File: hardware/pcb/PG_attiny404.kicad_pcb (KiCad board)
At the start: 2 copper layers, 20.3 x 59.7 mm, 28 parts, among them J1 0022232041, J2 Conn_01x01_Male, J3 Conn_01x01_Male, J4 Conn_01x01_Male, J5 Conn_01x01_Male, J6 Conn_01x01_Male, J7 Conn_01x01_Male, J8 Conn_01x01_Male, Q1 2N7002, SW1 SW_Push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

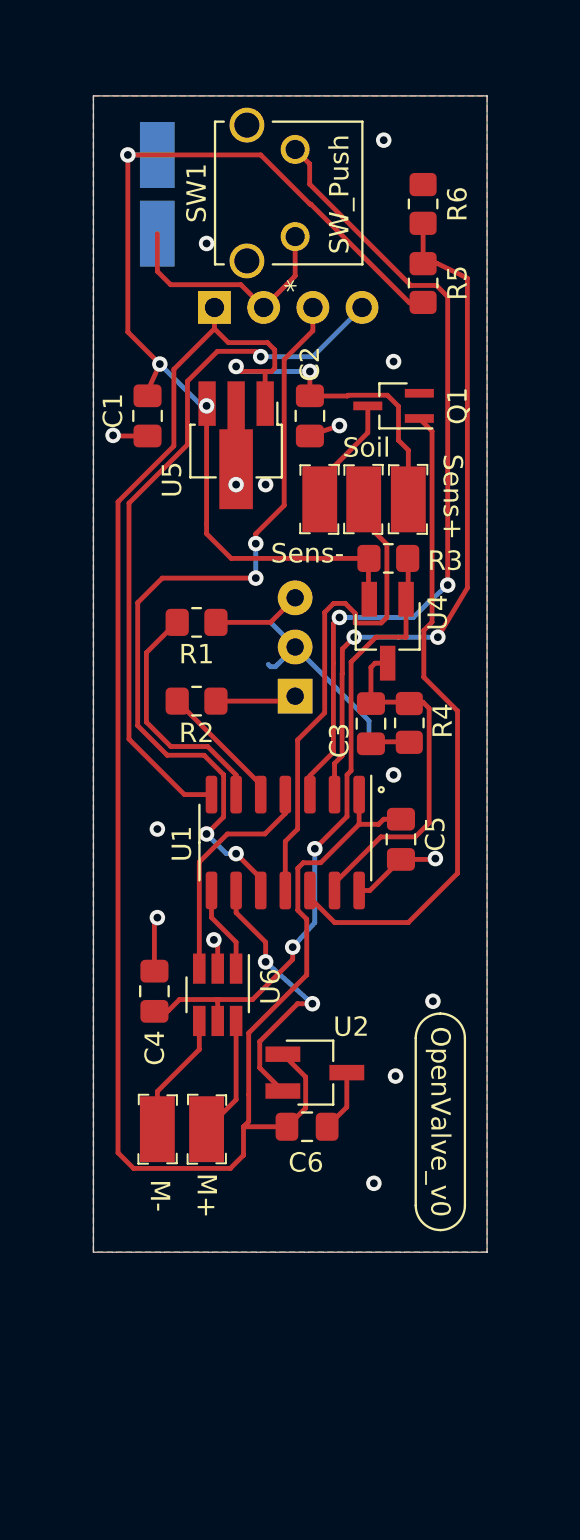
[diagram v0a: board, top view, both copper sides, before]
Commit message: Equiped PCB with additional led, changed other led, changed position of solder pads and side of hall sensor
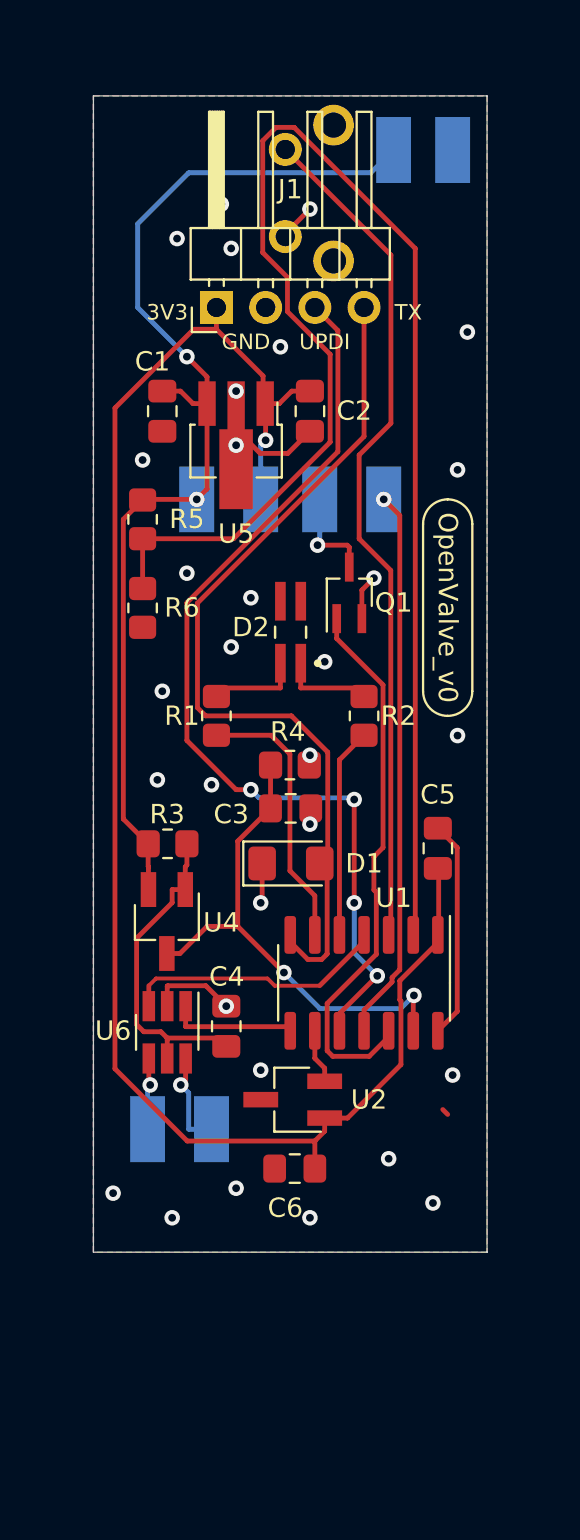
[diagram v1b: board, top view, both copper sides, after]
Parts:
- removed U3: XLUGR34M, LED_THT:LED_D3.0mm-3
- added D1: APTD3216QBC/D, LED_SMD:LED_1206_3216Metric_Pad1.42x1.75mm_HandSolder, F.Cu at (132.1, 106.9)
- added D2: XZMDKVG55W-8, XZMDKVG55W-8:LED_XZMDKVG55W-8, F.Cu at (132.1, 95.0)
- added J9: Conn_01x01_Male, digikey-footprints:PROBE_PAD_1206, B.Cu at (127.3, 88.1)
- J1: footprint Connector_PinSocket_2.54mm:PinSocket_1x04_P2.54mm_Horizontal -> Connector_PinHeader_2.54mm:PinHeader_1x04_P2.54mm_Horizontal; moved to F.Cu
- J4, J5, J6, J7, J8, SW1: moved to B.Cu
- R1, R2: value 100 Ohm -> 56 Ohm
- R5: value 200k -> 2M
- R6: value 100k -> 1M
- moved R6 25.4 mm to (124.5, 93.7), turned to -90 degrees
- moved R5 18.9 mm to (124.5, 89.2), turned to -90 degrees
- moved U4 18.8 mm to (125.7, 109.9)
- moved R3 18.6 mm to (125.7, 105.9)
- moved J2 15.8 mm to (140.5, 70.1)
- moved J3 12.2 mm to (137.4, 70.1)
- moved Q1 9.92 mm to (135.1, 93.0), turned to 90 degrees
- moved R2 8.68 mm to (135.9, 99.3), turned to -90 degrees
- moved U1 8.30 mm to (135.9, 113.1)
- moved J4 7.62 mm to (130.6, 88.1)
- moved R4 6.54 mm to (132.1, 101.9), turned to 180 degrees
- moved C3 6.02 mm to (132.1, 104.1), turned to 180 degrees
- moved R1 4.93 mm to (128.3, 99.3), turned to -90 degrees
- moved C4 4.13 mm to (128.8, 115.3)
- moved U6 3.25 mm to (125.7, 115.7)
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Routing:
- net /BatterySensing: track 36.3 -> 77.5 mm, vias 2 -> 0
- net +3V3: track 107.5 -> 85.2 mm, vias 2 -> 1
- net Net-(U4-Vs-): track 33.4 -> 17.0 mm, vias 2 -> 0
- net GND: track 44.5 -> 29.9 mm, vias 15 -> 31
- net /Hall: track 14.1 -> 2.82 mm, vias 2 -> 0
- net /UART_TX: track 36.0 -> 45.4 mm, vias 1 -> 0
- net /CurrentSensing: track 18.3 -> 26.2 mm, vias 0 -> 2
- net /UPDI: track 41.4 -> 49.2 mm
- net /SoilSensorOn: track 34.2 -> 28.6 mm
- net /LED_R: track 6.61 -> 10.8 mm
- net +BATT: track 54.1 -> 57.2 mm, vias 3 -> 2
- net Net-(J8-Pin_1): track 6.48 -> 3.74 mm, vias 0 -> 1
- net /Soilmoisture: track 26.0 -> 28.5 mm, vias 0 -> 1
- net /Motor+: track 4.56 -> 6.55 mm
- net /Motor-: track 12.0 -> 13.8 mm
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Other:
- board text added: "3.3V"
- board text added: "9V"
- board text removed: "G"
- board text removed: "R"
- board text removed: "Sens+"
- board text removed: "Sens-"

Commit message: Added Reverse voltage protection on PCB
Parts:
- added MOSFET1: SSM3J338R_LF, SOT23:SOT-23F_TOS-L, F.Cu at (124.8, 72.8)
- J1: footprint Connector_PinHeader_2.54mm:PinHeader_1x04_P2.54mm_Horizontal -> SOT23:PinHeader_1x04_P2.54mm_Horizontal_spezial
- R1, R2: value 56 Ohm -> 68 Ohm
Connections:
- J3 pad 1: +BATT -> Net-(J3-Pin_1)
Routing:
- net Net-(J3-Pin_1): track 0.00 -> 15.7 mm, vias 0 -> 1
- net +BATT: track 57.2 -> 45.1 mm, vias 2 -> 3

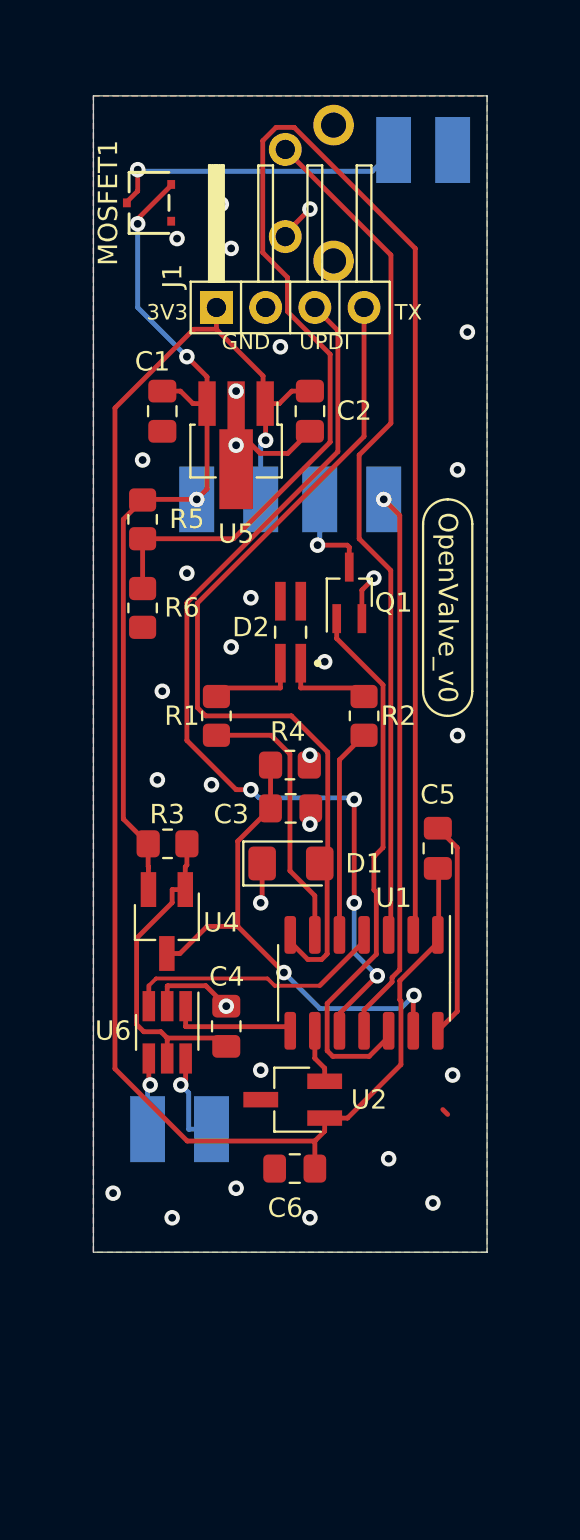
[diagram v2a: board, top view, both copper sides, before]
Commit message: Motor code polishing, Added p-channel to pcb for reverse voltage protection
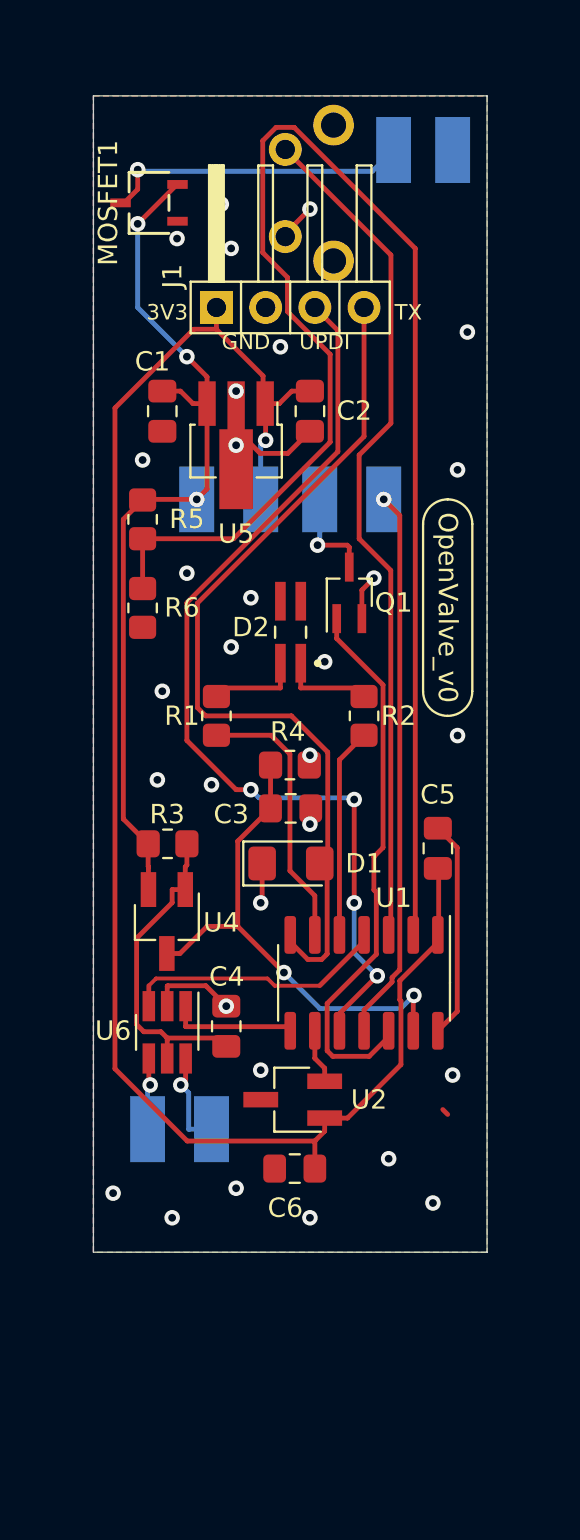
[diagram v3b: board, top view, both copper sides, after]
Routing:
- net GND: track 29.9 -> 30.6 mm

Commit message: New PCB Version 0.1
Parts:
- removed C6: 100nF, Capacitor_SMD:C_0805_2012Metric_Pad1.18x1.45mm_HandSolder
- removed U2: AH9246, Package_TO_SOT_SMD:SC-59_Handsoldering
- added F1: 0ZCG0075FF2C, 0ZCG0075FF2C:0ZCG0075FF2C, F.Cu at (126.4, 70.1)
- added R7: 10k, Resistor_SMD:R_0805_2012Metric_Pad1.20x1.40mm_HandSolder, F.Cu at (127.0, 127.8)
- added SW2: PTS526 SM15 SMTR2 LFS, PTS526_SK15_SMTR2_LFS:PTS526SK15SMTR2 LFS-M, F.Cu at (132.1, 130.3)
- added TVS1: SMF13A, SMF13A:SMFSeries_LTF, F.Cu at (125.2, 79.5)
- added TVS2: ESDA041-1JY, ESDA041-1JY:CR_041-1JY_STM, F.Cu at (138.5, 85.6)
- added TVS3: ESDA041-1JY, ESDA041-1JY:CR_041-1JY_STM, F.Cu at (132.9, 84.8)
- added TVS4: ESDA041-1JY, ESDA041-1JY:CR_041-1JY_STM, F.Cu at (135.4, 82.8)
- MOSFET1: footprint SOT23:SOT-23F_TOS-L -> SOT23:SOT-23F_TOS
- Q1: value 2N7002 -> 2N7002K-AU_R1_000A2; footprint Package_TO_SOT_SMD:SOT-323_SC-70_Handsoldering -> Package_TO_SOT_SMD:SOT-23_Handsoldering
- R1: value 68 Ohm -> 62 Ohm
- R2: value 68 Ohm -> 100 Ohm
- U1: value ATtiny404-SS -> ATtiny804-SS
- U4: footprint Package_TO_SOT_SMD:SC-59_Handsoldering -> Package_TO_SOT_SMD:SOT-23_Handsoldering
- U5: footprint Package_TO_SOT_SMD:SOT-89-3_Handsoldering -> Package_TO_SOT_SMD:SOT-89-3
- U6: footprint Package_TO_SOT_SMD:SOT-23-6_Handsoldering -> Package_TO_SOT_SMD:SOT-23-6
- moved C2 3.34 mm to (130.3, 81.8), turned to 0 degrees
- moved MOSFET1 1.84 mm to (125.2, 74.6), turned to 0 degrees
- moved R2 1.73 mm to (134.2, 98.8)
- moved R1 1.72 mm to (129.9, 98.8)
- moved R6 1.38 mm to (125.7, 93.2)
- moved R5 1.27 mm to (125.7, 89.2)
- moved C1 0.59 mm to (125.5, 84.2)
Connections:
- MOSFET1 pad 3: Net-(J3-Pin_1) -> Net-(F1-Pad2)
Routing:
- net +3V3: track 85.2 -> 106.2 mm, vias 1 -> 3
- net /Hall: track 2.82 -> 16.9 mm
- net Net-(J3-Pin_1): track 15.9 -> 9.39 mm
- net +BATT: track 45.5 -> 40.0 mm, vias 3 -> 1
- net /UART_TX: track 45.4 -> 40.9 mm
- net Net-(F1-Pad2): track 0.00 -> 3.91 mm
- net Net-(J5-Pin_1): track 5.12 -> 8.29 mm, vias 1 -> 2
- net /Soilmoisture: track 28.5 -> 31.3 mm
- net Net-(D2-Pad1): track 4.73 -> 2.11 mm
- net Net-(D2-Pad3): track 4.76 -> 2.16 mm
- net GND: track 30.6 -> 28.6 mm, vias 31 -> 43
- net /LED_G: track 14.1 -> 12.6 mm
- net /UPDI: track 49.2 -> 47.8 mm
- net /BatterySensing: track 77.5 -> 76.7 mm
- net Net-(U4-Vs-): track 17.0 -> 17.5 mm
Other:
- board size 20.3 x 59.7 mm -> 25.9 x 75.4 mm
- rule solder_mask_min_width: 0.25 -> 0.1
- board text added: "OpenValve_v0.1"
- board text removed: "9V"
- board text removed: "OpenValve_v0"

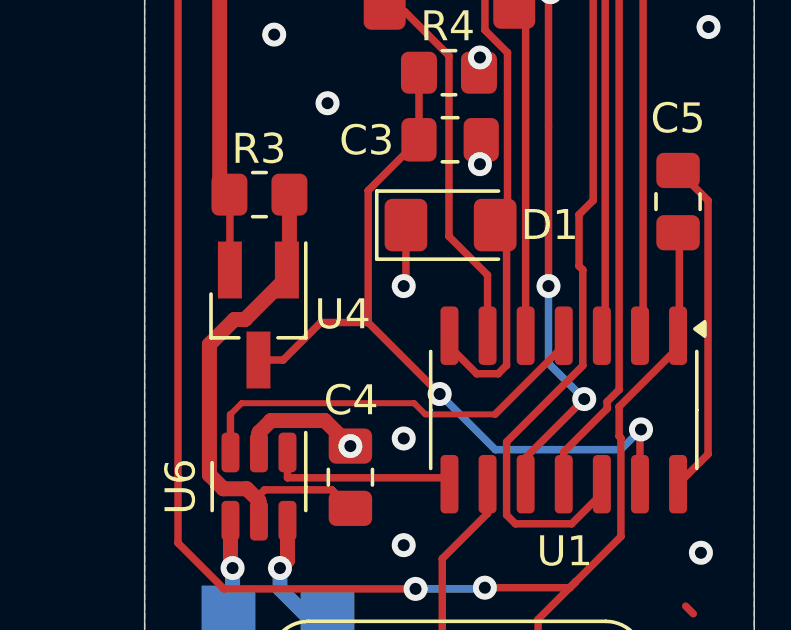
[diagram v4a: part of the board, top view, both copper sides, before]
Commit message: Footprint correction for Current Sensor
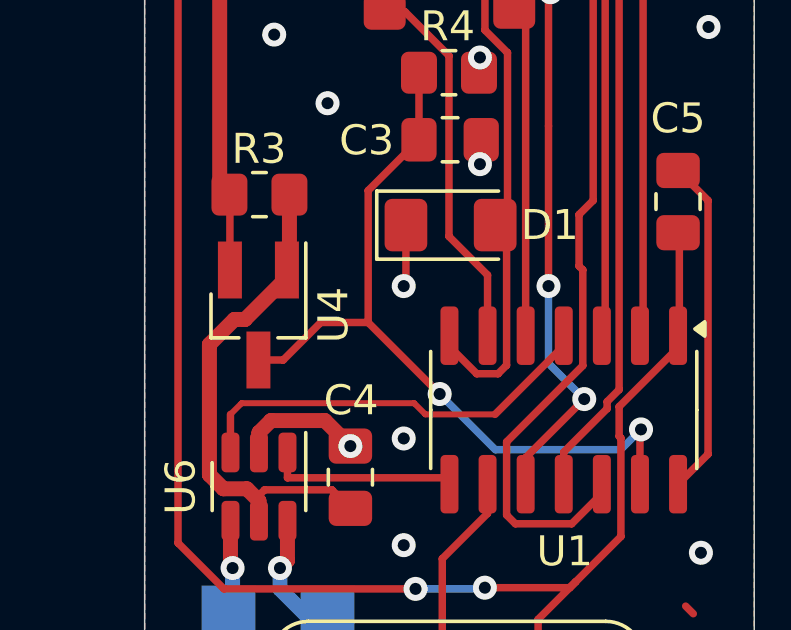
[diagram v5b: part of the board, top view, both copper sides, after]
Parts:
- U4: footprint Package_TO_SOT_SMD:SOT-23_Handsoldering -> ZXCT1009F:SOT-23_Handsoldering_ZXCT1009F
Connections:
- U4 pad 1: Net-(U4-Vs-) -> /CurrentSensing
- U4 pad 3: /CurrentSensing -> Net-(U4-Vs-)
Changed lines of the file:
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@@
 		)
 	)
-	(footprint "Package_TO_SOT_SMD:SOT-23_Handsoldering"
+	(footprint "ZXCT1009F:SOT-23_Handsoldering_ZXCT1009F"
 		(layer "F.Cu")
 		(at 125.7116 109.9302 -90)
@@
 		(tags "SOT-23")
 		(property "Reference" "U4"
-			(at -0.0202 -2.8084 0)
+			(at 0 -2.5 270)
 			(layer "F.SilkS")
 			(effects
@@
 		)
 		(property "Value" "ZXCT1009F"
-			(at -0.2202 6.1916 0)
+			(at 0 2.5 270)
 			(layer "F.Fab")
 			(effects
@@
 		)
 		(pad "1" smd rect
-			(at -1.5 -0.95 270)
+			(at 1.5 0 270)
 			(size 1.9 0.8)
 			(layers "F.Cu" "F.Mask" "F.Paste")
-			(net 16 "Net-(U4-Vs-)")
-			(pinfunction "Vs-")
-			(pintype "input")
+			(net 4 "/CurrentSensing")
+			(pinfunction "Iout")
+			(pintype "output")
 		)
 		(pad "2" smd rect
@@
 		)
 		(pad "3" smd rect
-			(at 1.5 0 270)
+			(at -1.5 -0.95 270)
 			(size 1.9 0.8)
 			(layers "F.Cu" "F.Mask" "F.Paste")
-			(net 4 "/CurrentSensing")
-			(pinfunction "Iout")
-			(pintype "output")
+			(net 16 "Net-(U4-Vs-)")
+			(pinfunction "Vs-")
+			(pintype "input")
 		)
 		(embedded_fonts no)

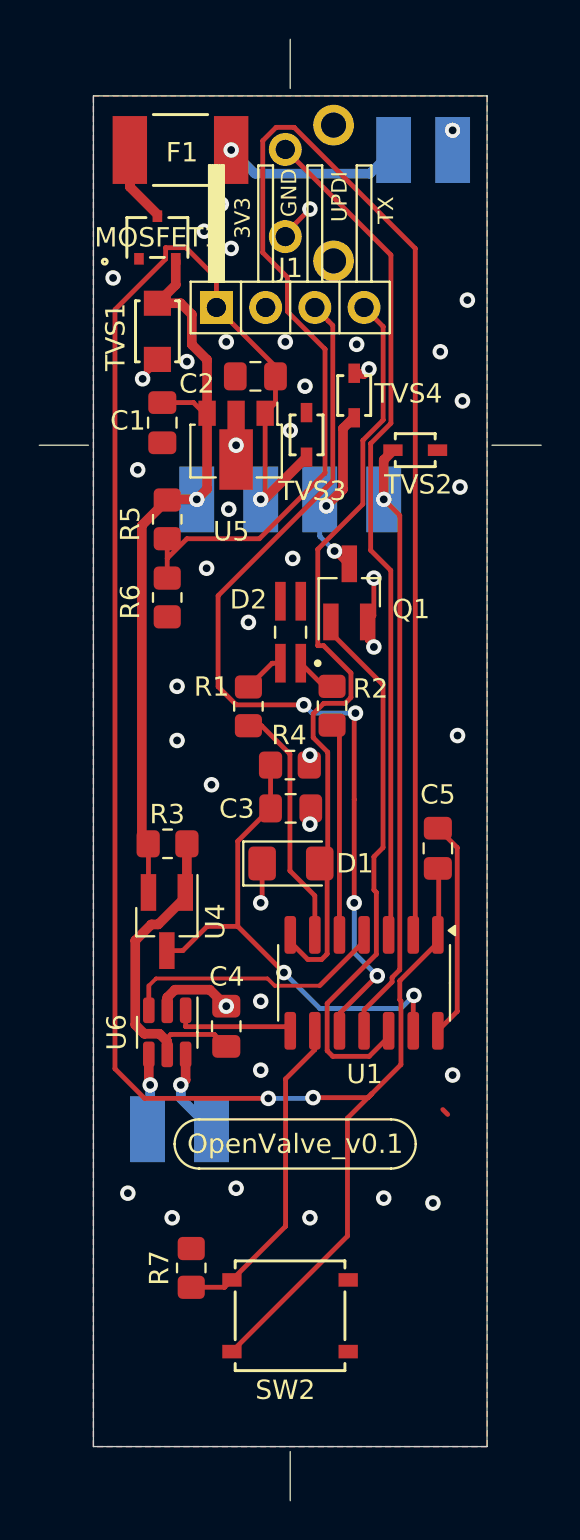
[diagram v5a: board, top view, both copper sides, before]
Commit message: Added new motor driver to pcb
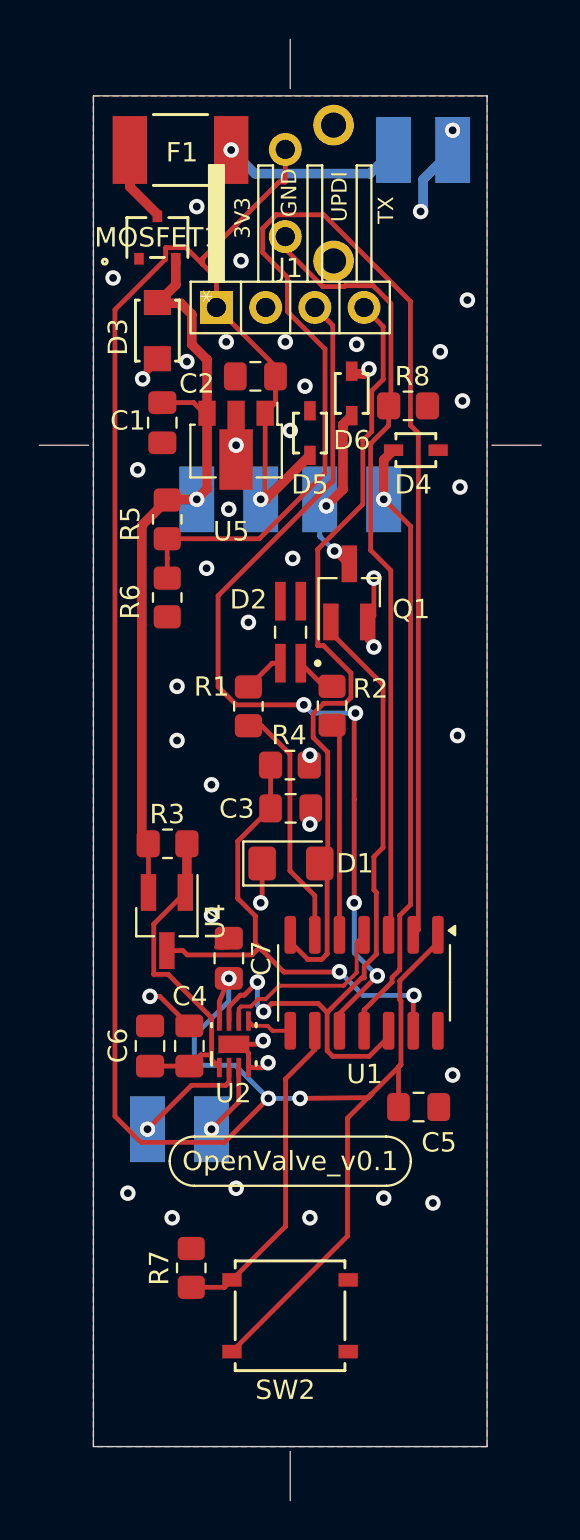
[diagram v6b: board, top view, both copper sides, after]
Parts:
- removed TVS1: SMF13A, SMF13A:SMFSeries_LTF
- removed TVS2, TVS3, TVS4: ESDA041-1JY, ESDA041-1JY:CR_041-1JY_STM
- removed U6: MP6513GJ, Package_TO_SOT_SMD:SOT-23-6
- added C6: 100nF, Capacitor_SMD:C_0805_2012Metric_Pad1.18x1.45mm_HandSolder, F.Cu at (124.8, 116.4)
- added C7: 100nF, Capacitor_SMD:C_0805_2012Metric_Pad1.18x1.45mm_HandSolder, F.Cu at (128.9, 111.8)
- added D3: SMF13A, SMF13A:SMFSeries_LTF, F.Cu at (125.2, 79.4)
- added D4: ESDA041-1JY, ESDA041-1JY:CR_041-1JY_STM, F.Cu at (138.6, 85.6)
- added D5: ESDA041-1JY, ESDA041-1JY:CR_041-1JY_STM, F.Cu at (133.1, 84.7)
- added D6: ESDA041-1JY, ESDA041-1JY:CR_041-1JY_STM, F.Cu at (135.3, 82.7)
- added R8: 10k, Resistor_SMD:R_0805_2012Metric_Pad1.20x1.40mm_HandSolder, F.Cu at (138.2, 83.3)
- added U2: DRV8837DSGR, DRV8837DSGR:DRV8837DSGR_NV, F.Cu at (129.2, 116.3)
- moved C5 13.4 mm to (138.7, 119.5), turned to 180 degrees
- moved C4 2.16 mm to (126.9, 116.4)
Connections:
- SW1 pad 1: GND -> /MotorStop
- SW1 pad 2: /MotorStop -> +3V3
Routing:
- net +3V3: track 106.2 -> 129.0 mm, vias 3 -> 4
- net /SoilSensorOn: track 28.6 -> 36.7 mm, vias 0 -> 2
- net /BatterySensing: track 76.7 -> 69.1 mm
- net GND: track 28.6 -> 22.7 mm
- net /Motor+: track 6.55 -> 2.37 mm
- net /Motor-: track 13.8 -> 10.3 mm
- net /MotorStop: track 43.7 -> 41.0 mm
- net Net-(J8-Pin_1): track 4.12 -> 6.34 mm
- net Net-(J7-Pin_1): track 4.62 -> 3.77 mm
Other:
- rule pad_to_mask_clearance: 0.051 -> 0.05

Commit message: Small Changes for Ordering PCB
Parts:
- added J10: Cap +, digikey-footprints:PROBE_PAD_0603, B.Cu at (124.7, 117.3)
- added J11: Cap -, digikey-footprints:PROBE_PAD_0603, B.Cu at (124.7, 115.3)
- R8: value 10k -> 220k
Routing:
- net Net-(J10-Pin_1): vias 0 -> 1
- net GND: vias 43 -> 44
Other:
- board size 25.9 x 75.4 mm -> 20.3 x 69.7 mm
- board text added: "Cap+"
- board text added: "Cap-"
- board text added: "OpenValve_v0.2"
